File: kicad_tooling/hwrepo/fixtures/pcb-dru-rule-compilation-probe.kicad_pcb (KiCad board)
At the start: 2 copper layers, 30 x 20 mm, 0 parts

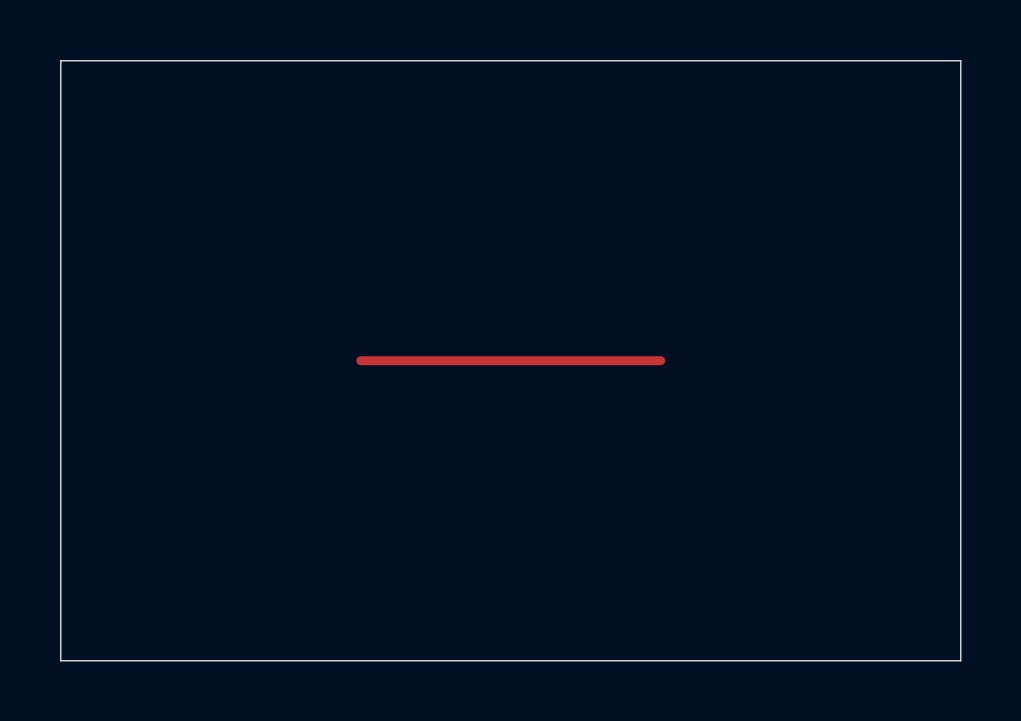
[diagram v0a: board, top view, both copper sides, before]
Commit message: test(pcb): prove DRC rule load with named clearance
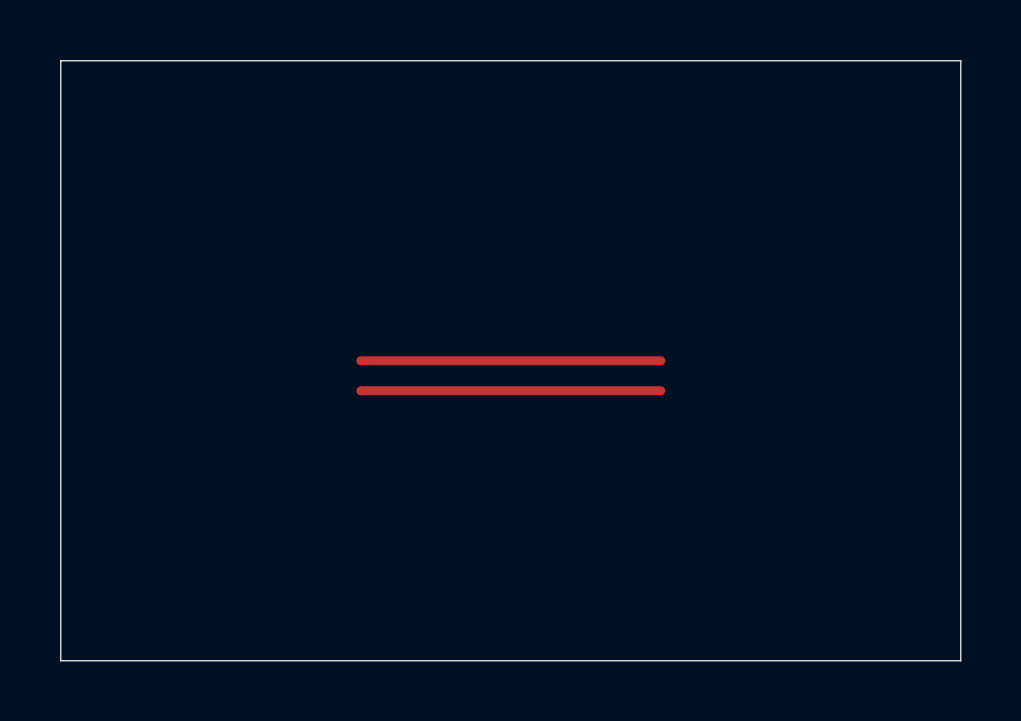
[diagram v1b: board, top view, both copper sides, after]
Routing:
- net KTT_DRC_RULE_PROBE_PEER: track 0.00 -> 10.0 mm
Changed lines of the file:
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@@
   (net 0 "")
   (net 1 "KTT_DRC_RULE_PROBE")
+  (net 2 "KTT_DRC_RULE_PROBE_PEER")
   (segment (start 10 10) (end 20 10) (width 0.3) (layer "F.Cu") (net 1)
 )
+  (segment (start 10 11) (end 20 11) (width 0.3) (layer "F.Cu") (net 2)
+)
   (gr_rect (start 0 0) (end 30 20)
